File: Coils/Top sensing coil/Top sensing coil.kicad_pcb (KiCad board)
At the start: 2 copper layers, 74.9 x 56.5 mm, 7 parts, among them J1 Conn_01x02_Pin, J2 Conn_01x02_Socket

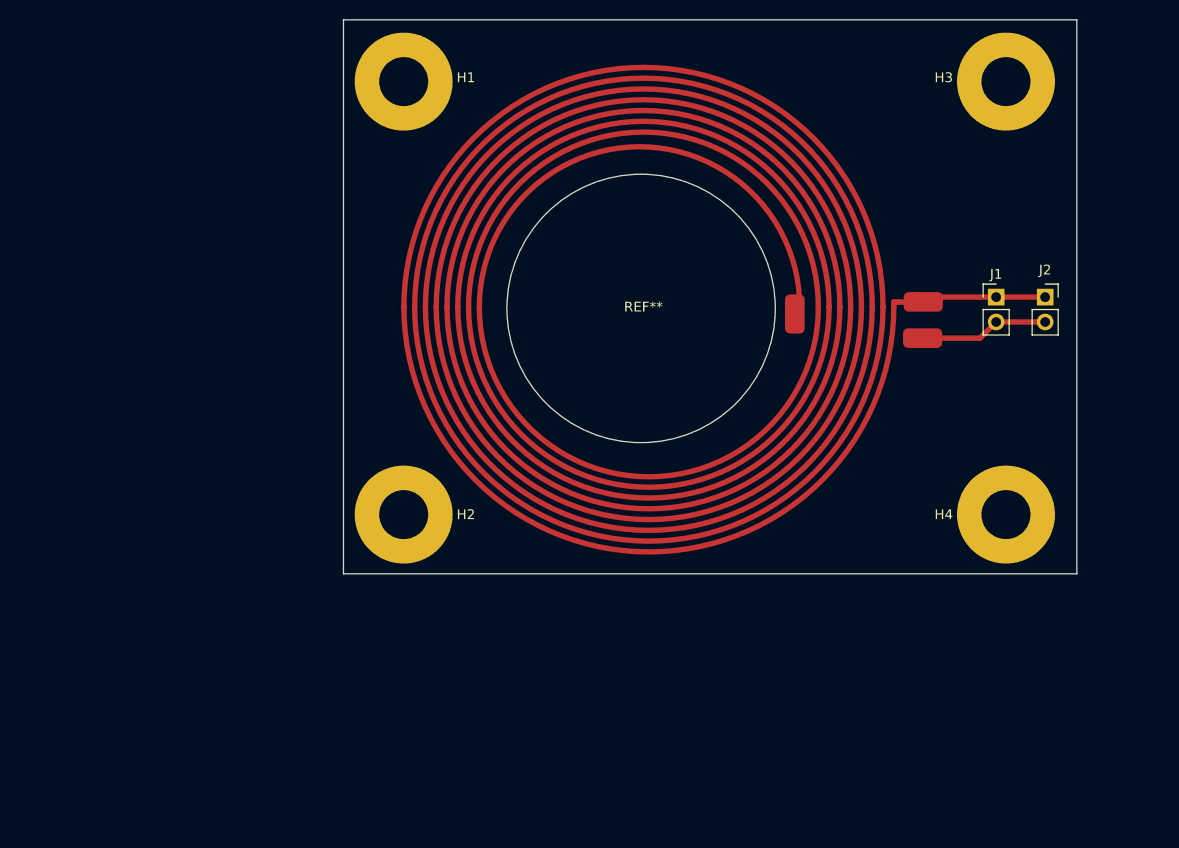
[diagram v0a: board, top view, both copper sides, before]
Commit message: added 3d models for OPA3692, THS3091 and BNC connector
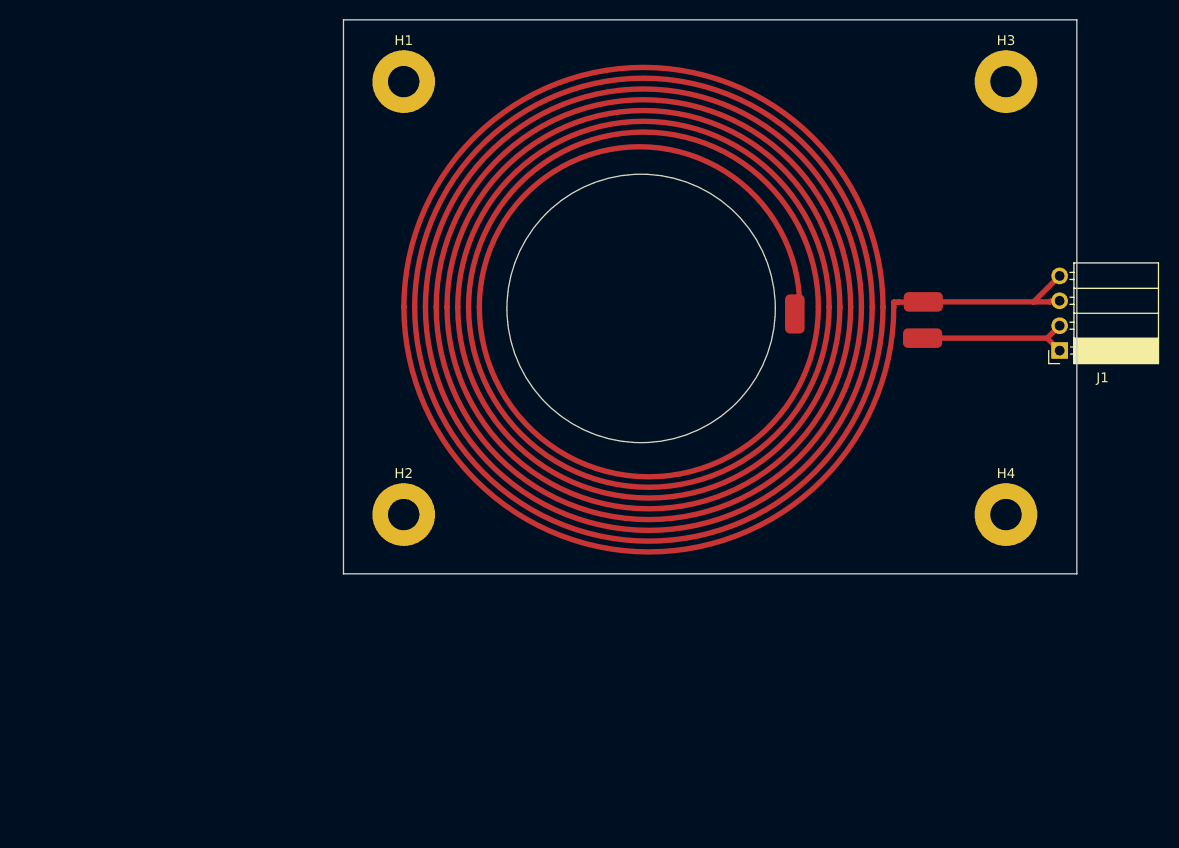
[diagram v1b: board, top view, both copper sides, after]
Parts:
- removed J2: Conn_01x02_Socket, Connector_PinSocket_2.54mm:PinSocket_1x02_P2.54mm_Vertical
- H1, H2, H3, H4: footprint MountingHole:MountingHole_5mm_Pad -> MountingHole:MountingHole_3.2mm_M3_Pad
- J1: value Conn_01x02_Pin -> Conn_01x04_Socket; footprint Connector_PinHeader_2.54mm:PinHeader_1x02_P2.54mm_Vertical -> Connector_PinSocket_2.54mm:PinSocket_1x04_P2.54mm_Horizontal
- moved J1 8.47 mm to (243.5, 106.5), turned to 180 degrees
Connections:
- J1 pad 1: /coil start -> /coil end
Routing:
- net /coil start: track 13.4 -> 18.4 mm
- net /coil end: track 13.9 -> 16.3 mm

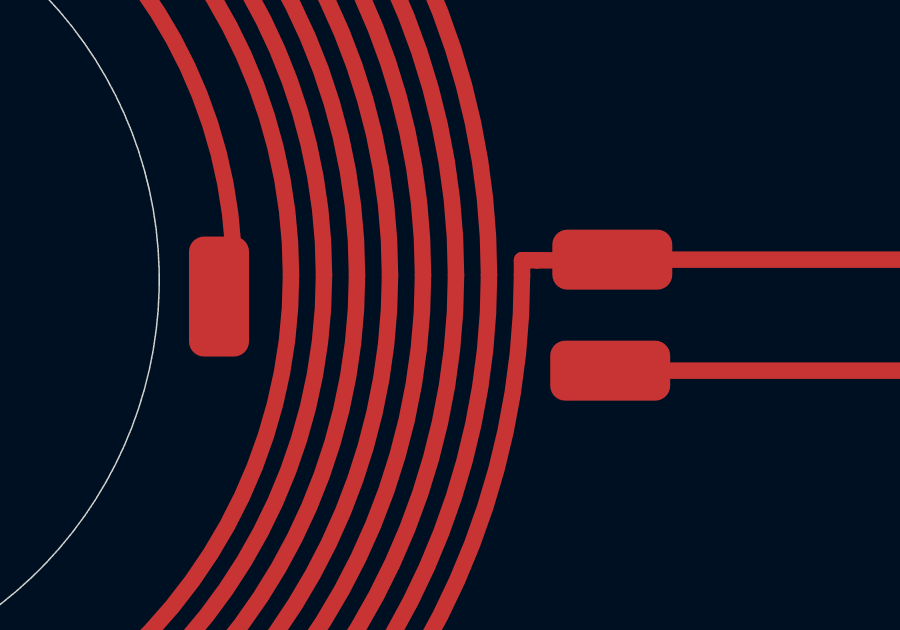
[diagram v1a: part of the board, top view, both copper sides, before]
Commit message: Small corrections, changed footprint for edge SMA connectors
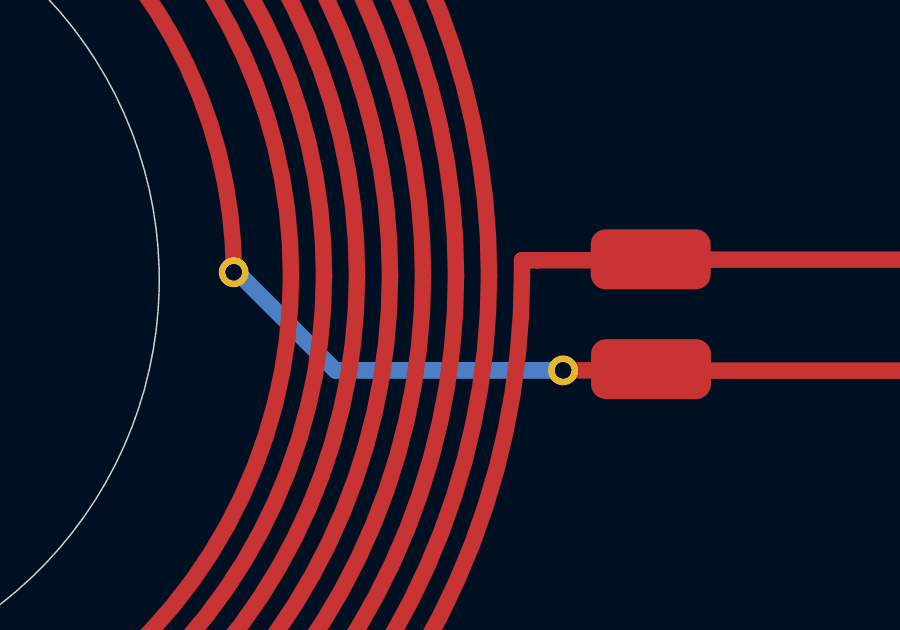
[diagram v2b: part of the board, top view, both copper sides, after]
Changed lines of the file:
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@@
 		(fp_line
 			(start 26.05 -0.5)
-			(end 27.22 -0.49)
+			(end 28.87 -0.5)
+			(stroke
+				(width 0.55)
+				(type default)
+			)
+			(layer "F.Cu")
+		)
+		(fp_line
+			(start 26.92 3.17)
+			(end 26.92 3.17)
+			(stroke
+				(width 0.55)
+				(type default)
+			)
+			(layer "F.Cu")
+			(net 4784199)
+		)
+		(fp_line
+			(start 26.92 3.17)
+			(end 29.12 3.17)
 			(stroke
 				(width 0.55)
@@
 			(layer "F.Cu")
 		)
-		(pad "" smd roundrect
-			(at 15.45 0.71 90)
-			(size 4 2)
-			(layers "F.Cu")
-			(roundrect_rratio 0.25)
+		(fp_line
+			(start 19.33 3.17)
+			(end 15.94 -0.22)
+			(stroke
+				(width 0.55)
+				(type default)
+			)
+			(layer "B.Cu")
+		)
+		(fp_line
+			(start 26.92 3.17)
+			(end 19.33 3.17)
+			(stroke
+				(width 0.55)
+				(type default)
+			)
+			(layer "B.Cu")
+		)
+		(fp_line
+			(start 26.92 3.17)
+			(end 26.92 3.17)
+			(stroke
+				(width 0.55)
+				(type default)
+			)
+			(layer "B.Cu")
+		)
+		(pad "" thru_hole circle
+			(at 15.94 -0.1 90)
+			(size 1 1)
+			(drill 0.55)
+			(layers "*.Cu" "*.Mask")
+			(remove_unused_layers no)
+		)
+		(pad "" thru_hole circle
+			(at 26.92 3.17 90)
+			(size 1 1)
+			(drill 0.55)
+			(layers "*.Cu" "*.Mask")
+			(remove_unused_layers no)
 		)
 		(pad "1" smd roundrect
-			(at 28.56 -0.52)
+			(at 29.84 -0.53)
 			(size 4 2)
 			(layers "F.Cu")
@@
 		)
 		(pad "2" smd roundrect
-			(at 28.49 3.18)
+			(at 29.85 3.13)
 			(size 4 2)
 			(layers "F.Cu")
@@
 		)
 		(fp_text user "${REFERENCE}"
-			(at -5.775 3.81 270)
-			(layer "F.Fab")
-			(effects
+			(at -5.775 3.81 -90)
+			(layer "F.Fab")
+			(effects

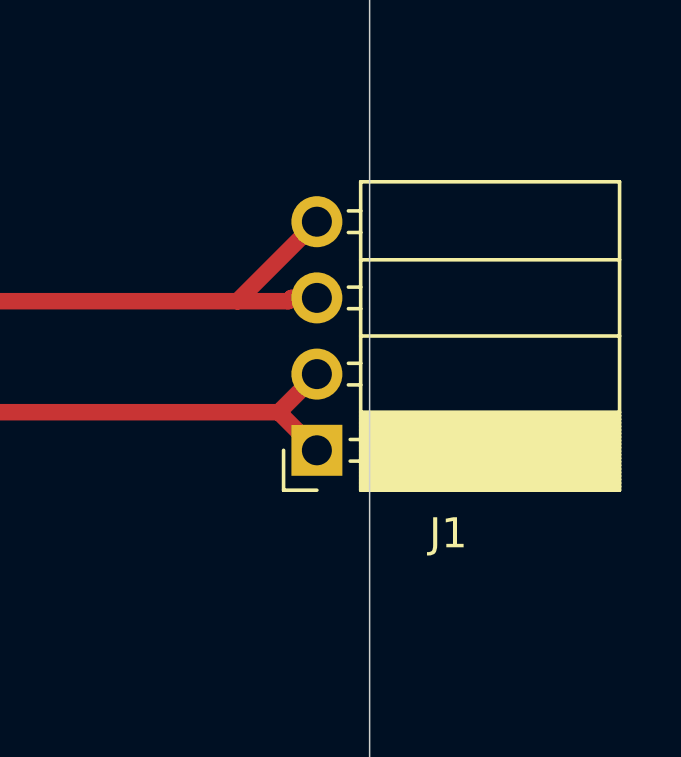
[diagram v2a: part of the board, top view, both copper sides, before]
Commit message: Added via stiching to TX board, moved almost all vias off of pads, increased the trace width for the power supply and changed coil connector to horizontal socket
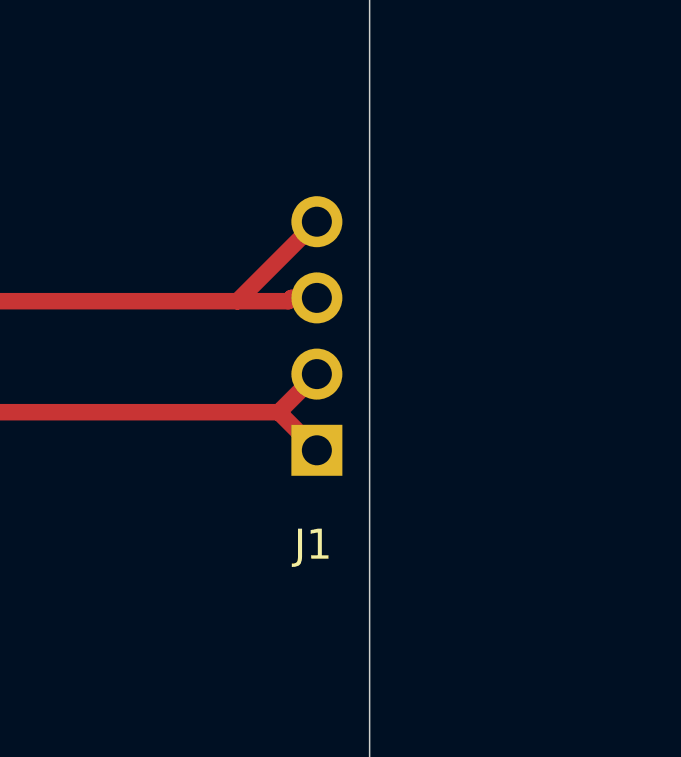
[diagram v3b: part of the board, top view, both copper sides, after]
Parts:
- J1: value Conn_01x04_Socket -> Conn_01x04; footprint Connector_PinSocket_2.54mm:PinSocket_1x04_P2.54mm_Horizontal -> Connector_PinHeader_2.54mm:PinHeader_1x04_P2.54mm_Horizontal; moved to B.Cu
- turned J1 to 0 degrees

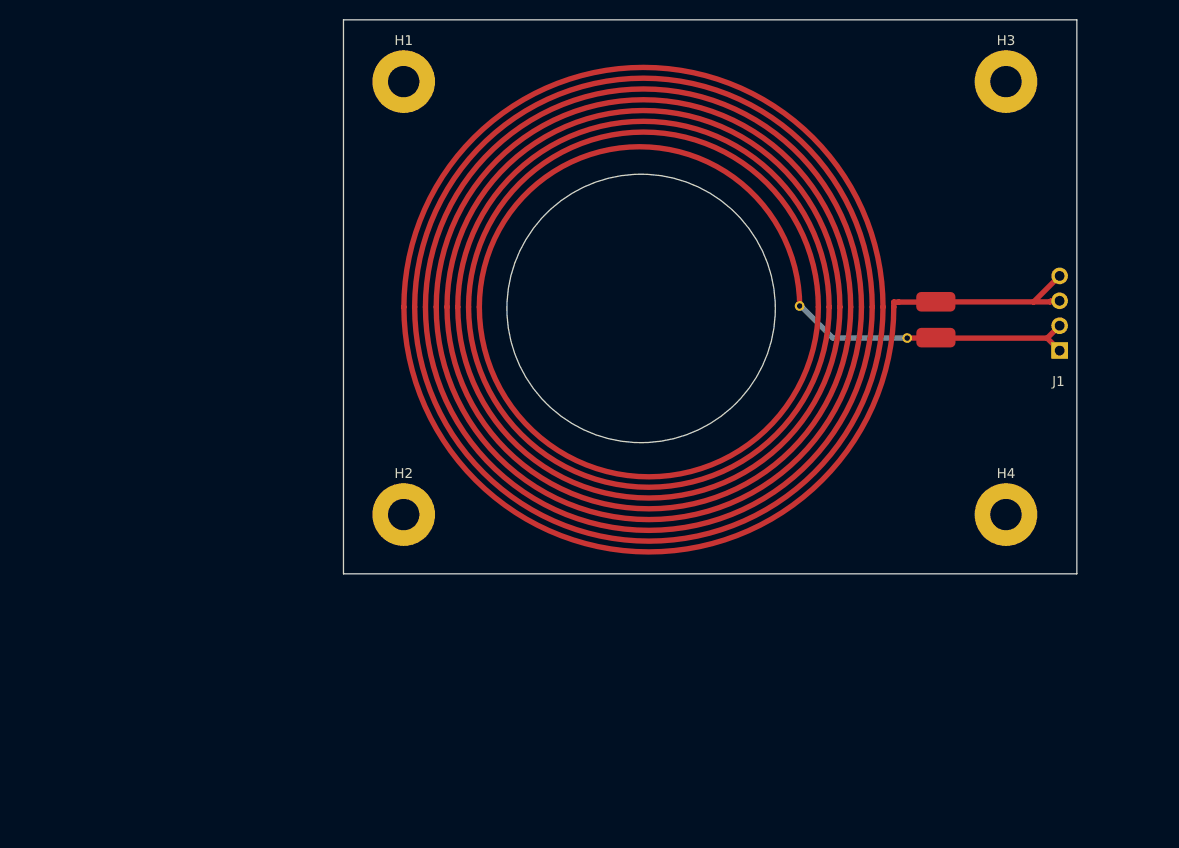
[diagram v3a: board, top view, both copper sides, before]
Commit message: Drew a footprint for a BNC edge connector 112640, made sure coils are centered and as symmetrical as possible:wq
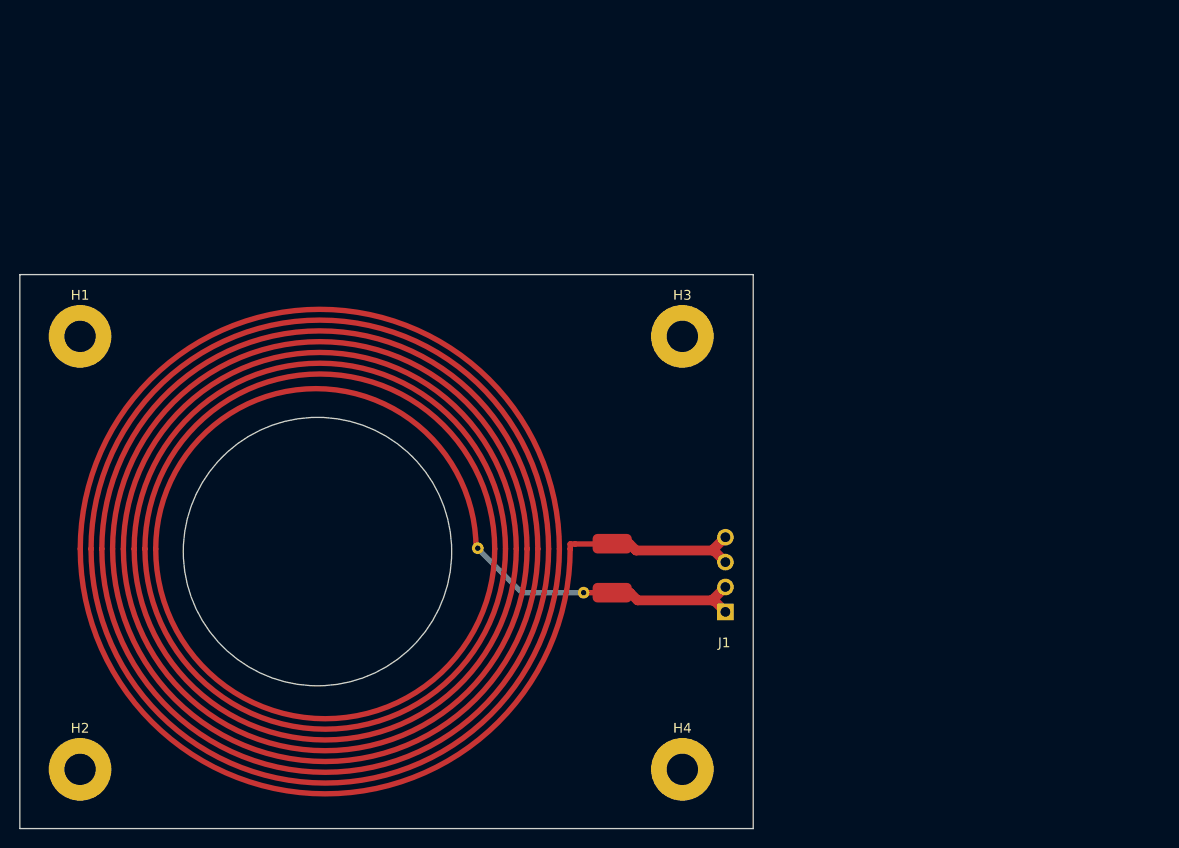
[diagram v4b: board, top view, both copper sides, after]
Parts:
- moved J1 43.3 mm to (209.4, 133.1)
- moved H1 42.0 mm to (143.5, 105.0)
- moved H2 42.0 mm to (143.5, 149.2)
- moved H3 42.0 mm to (205.0, 105.0)
- moved H4 42.0 mm to (205.0, 149.2)
- moved REF** 41.2 mm to (168.0, 126.7)
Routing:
- net /coil start: track 18.4 -> 14.3 mm
- net /coil end: track 16.3 -> 14.2 mm
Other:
- outline, holes or cut-outs redrawn

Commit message: Final version before review 3
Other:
- board size 74.9 x 56.5 mm -> 74.8 x 56.5 mm
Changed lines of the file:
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@@
 		)
 	)
-	(gr_rect
-		(start 137.3532 98.6948)
-		(end 212.2032 155.2352)
-		(stroke
-			(width 0.05)
-			(type default)
-		)
-		(fill none)
+	(gr_line
+		(start 143.526275 155.215527)
+		(end 206.030125 155.215527)
+		(stroke
+			(width 0.05)
+			(type default)
+		)
+		(layer "Edge.Cuts")
+	)
+	(gr_arc
+		(start 143.526275 155.215527)
+		(mid 139.170125 153.41115)
+		(end 137.365748 149.055)
+		(stroke
+			(width 0.05)
+			(type default)
+		)
+		(layer "Edge.Cuts")
+	)
+	(gr_arc
+		(start 137.365748 104.875)
+		(mid 139.170125 100.51885)
+		(end 143.526275 98.714473)
+		(stroke
+			(width 0.05)
+			(type default)
+		)
+		(layer "Edge.Cuts")
+	)
+	(gr_line
+		(start 143.526275 98.714473)
+		(end 206.030125 98.714473)
+		(stroke
+			(width 0.05)
+			(type default)
+		)
+		(layer "Edge.Cuts")
+	)
+	(gr_line
+		(start 137.365748 149.055)
+		(end 137.365748 104.875)
+		(stroke
+			(width 0.05)
+			(type default)
+		)
+		(layer "Edge.Cuts")
+	)
+	(gr_arc
+		(start 206.030125 98.714473)
+		(mid 210.386228 100.518882)
+		(end 212.190652 104.875)
+		(stroke
+			(width 0.05)
+			(type default)
+		)
+		(layer "Edge.Cuts")
+	)
+	(gr_line
+		(start 212.190652 104.875)
+		(end 212.190652 149.055)
+		(stroke
+			(width 0.05)
+			(type default)
+		)
 		(layer "Edge.Cuts")
 	)
@@
 		)
 		(fill none)
+		(layer "Edge.Cuts")
+	)
+	(gr_arc
+		(start 212.190652 149.055)
+		(mid 210.386284 153.411159)
+		(end 206.030125 155.215527)
+		(stroke
+			(width 0.05)
+			(type default)
+		)
 		(layer "Edge.Cuts")
 	)
@@
 		(net 2)
 	)
+	(group ""
+		(members "08a3f0d5-a46f-4cde-8c0d-88d9134f8d28" "09948556-46c6-49ab-82b8-aba3c511a158"
+			"23911289-217c-4660-a974-185445f8a3e0" "31b7a3c4-fb38-4113-9120-11d65654b4e0"
+			"37576dd5-c50e-4344-8a90-75fe318802da" "43cbfbf4-3374-4ed2-9d1c-b9bd4852660f"
+			"5080a880-8a2f-474c-8135-a668a2582266" "5557cbad-b761-4f2d-9a96-a30c43214de2"
+			"58c5db71-fcf1-44d1-a90a-382357d93bfb" "67dea639-4b07-4257-9dff-5a9fa080f34a"
+			"721fa5f7-7e32-45b0-9d40-280d08cc6881" "7977b479-71e2-4015-ae86-58200bc51bc7"
+			"79deb950-147f-4d4e-a2c0-d32b38151961" "8d5d346f-9d18-439b-a822-4c5cc8bbd23c"
+			"9bda4fe9-dc86-4f3e-a409-b6f7802714ef" "b055f1b0-442a-41ca-897b-1c0235c82a6d"
+			"b73963cd-3e65-4c45-811f-c40946bec380" "c19436dd-51fb-43ca-a9c3-9892434a5fdc"
+			"c5d7f96e-0b21-41a5-b1bb-0ae3b8429339" "ccbf297f-60a7-4df8-ae07-cadfbbce576e"
+			"d5148b71-c2f1-4752-b5a8-a2cc4f6f9f0a" "dce28e18-7bcd-48bf-8584-020020bd9bb5"
+			"e70e1a24-5552-483a-b8bb-f1d9f8a4c234" "fb16baa9-755b-4fd0-9aa9-73a06fd576c7"
+			"fbea5557-41fc-41b0-83e2-b3a1160f0a00"
+		)
+	)
+	(group ""
+		(members "0bfe96e1-0225-427c-b361-7fda94d4de84" "0cff42cd-d7da-4f80-a451-8177ceab42e9"
+			"6420dd52-245c-47ca-8408-009ed6ec2aaf" "9995c011-8855-4e11-acc5-1929c1d93b0f"
+			"c4f64d7e-d77e-4486-81f7-e2f783a5c9d1" "dbf2c700-fada-4671-862e-d15f73b34b14"
+			"e16aa492-be6a-4533-9fd8-78870c7a2376" "ff0a85c8-3821-4a2b-b66c-44d32baef268"
+		)
+	)
 )
